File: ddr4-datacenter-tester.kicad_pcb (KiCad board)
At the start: 8 copper layers, 152.9 x 90 mm, 379 parts, among them IC1 TPS54561, IC3 TPD8S009DSMR, J1 0878311420, J10 61300311121, J3 DC_SOCKET, J4 WE_629105150521, J5 2309409-1, J6 685119134923, J7 1140084168, J8 61300311121, Q2 BSS138APW, Q3 BSS138APW, Q4 BSS138APW, Q5 BSS138APW, Q6 BSS138APW, Q7 BSS138APW, Q8 BSS138APW, U1 XC7K70T-FBG484, U10 LM3881MME_NOPB, U11 S27KL0641DABHI023, U12 TPS62823DLCT, U13 XC7K160T-2FFG676C, U14 2199155-1, U15 XC7K160T-FFG676, U16 XC7K70T-FBG484, U2 ASFLMB-100.000MHZ-XY-T, U3 S25FL128SAGNFI000, U4 TPS65296, U5 TPS62823DLCT, U6 KSZ9031RNXCA, U7 FT4232HQ, U8 SRST, U9 TPS62823DLCT, Y1 ABM8G-25.000MHZ-18-D2Y-T, Y2 ABM8G-12.000MHZ-18-D2Y-T

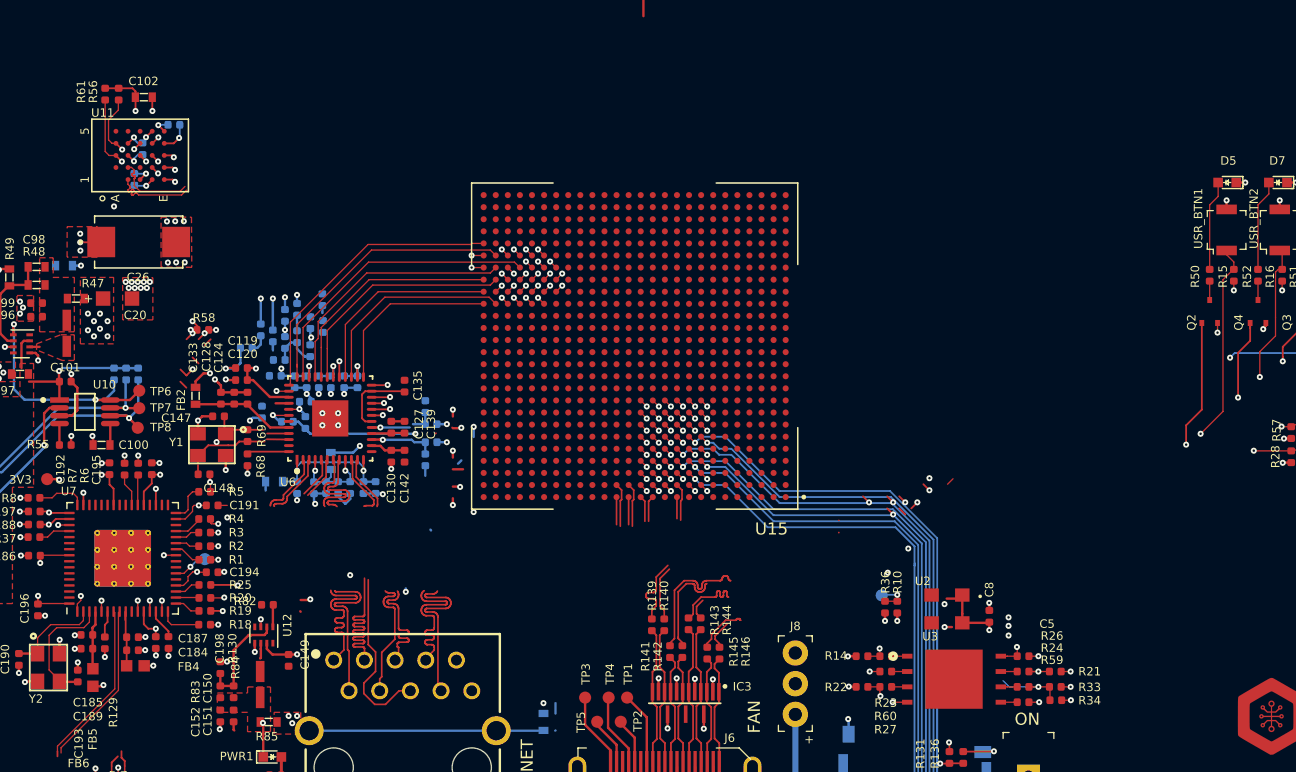
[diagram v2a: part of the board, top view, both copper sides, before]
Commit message: Connect QSPI (fix), GPIOs, JTAG, HR, UART
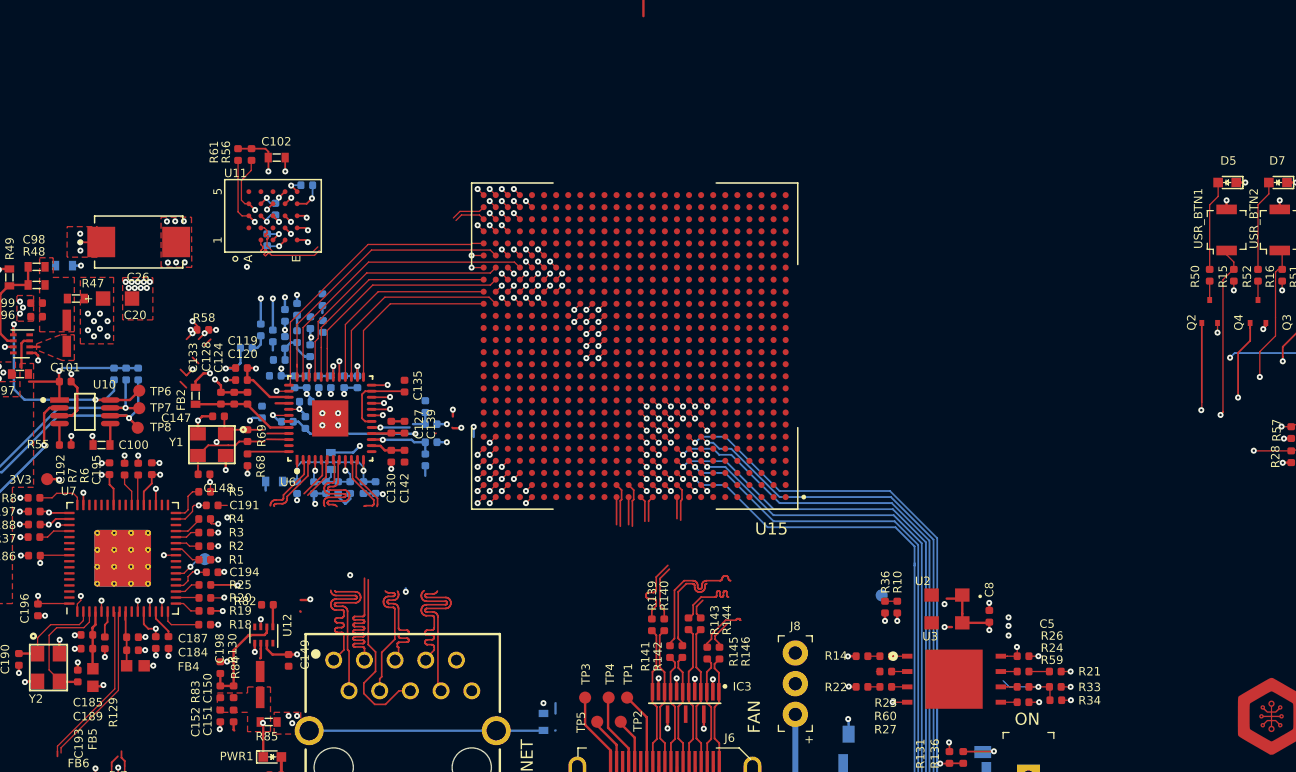
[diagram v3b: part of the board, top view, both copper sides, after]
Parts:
- moved C102 12.1 mm to (154.0, 74.5)
- moved C103 12.1 mm to (156.5, 76.7)
- moved C104 12.1 mm to (153.2, 81.3)
- moved C105 12.1 mm to (153.9, 78.7)
- moved R56 12.1 mm to (151.9, 74.2)
- moved R61 12.1 mm to (150.8, 74.2)
- moved U11 12.1 mm to (153.7, 79.3)
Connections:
- U15 pad A22: Net-(U15-PadA22) -> QSPI_DQ3
- U15 pad A25: Net-(U15-PadA25) -> QSPI_DQ1
- U15 pad AC24: Net-(U15-PadAC24) -> HR_RST
- U15 pad AC26: Net-(U15-PadAC26) -> HR_CS
- U15 pad AD23: Net-(U15-PadAD23) -> HR_RW
- U15 pad AD24: Net-(U15-PadAD24) -> HR_DQ7
- U15 pad AD25: Net-(U15-PadAD25) -> HR_DQ1
- U15 pad AD26: Net-(U15-PadAD26) -> HR_CKP
- U15 pad AE22: Net-(U15-PadAE22) -> HR_DQ3
- U15 pad AE23: Net-(U15-PadAE23) -> HR_DQ0
- U15 pad AE25: Net-(U15-PadAE25) -> HR_DQ6
- U15 pad AE26: Net-(U15-PadAE26) -> HR_CKN
- U15 pad AF23: Net-(U15-PadAF23) -> HR_DQ4
- U15 pad AF24: Net-(U15-PadAF24) -> HR_DQ2
- U15 pad AF25: Net-(U15-PadAF25) -> HR_DQ5
- U15 pad B22: Net-(U15-PadB22) -> QSPI_DQ2
- U15 pad B24: Net-(U15-PadB24) -> QSPI_DQ0
- U15 pad B25: Net-(U15-PadB25) -> PUDC_B
- U15 pad B26: Net-(U15-PadB26) -> EMCCLK
- U15 pad C23: Net-(U15-PadC23) -> FCS_B
- U15 pad C24: Net-(U15-PadC24) -> AUX_JTAG_TCK
- U15 pad C26: Net-(U15-PadC26) -> AUX_JTAG_TDO
- U15 pad D11: FCS_B -> Net-(U15-PadD11)
- U15 pad D24: Net-(U15-PadD24) -> AUX_JTAG_TDI
- U15 pad D25: Net-(U15-PadD25) -> AUX_JTAG_TMS
- U15 pad D26: Net-(U15-PadD26) -> UART1_TX
- U15 pad E11: PUDC_B -> Net-(U15-PadE11)
- U15 pad E25: Net-(U15-PadE25) -> UART1_RX
- U15 pad E26: Net-(U15-PadE26) -> UART0_TX
- U15 pad F10: QSPI_DQ1 -> Net-(U15-PadF10)
- U15 pad F25: Net-(U15-PadF25) -> UART0_RX
- U15 pad G10: QSPI_DQ0 -> Net-(U15-PadG10)
- U15 pad G9: QSPI_DQ2 -> Net-(U15-PadG9)
- U15 pad H8: QSPI_DQ3 -> Net-(U15-PadH8)
- U15 pad N16: Net-(U15-PadN16) -> USR_BTN1
- U15 pad N17: Net-(U15-PadN17) -> USR_LED1
- U15 pad P16: Net-(U15-PadP16) -> USR_LED5
- U15 pad R16: Net-(U15-PadR16) -> USR_LED2
- U15 pad R17: Net-(U15-PadR17) -> USR_BTN4
- U15 pad T17: Net-(U15-PadT17) -> USR_LED4
- U15 pad T18: Net-(U15-PadT18) -> USR_BTN3
- U15 pad U16: Net-(U15-PadU16) -> USR_LED3
- U15 pad U17: Net-(U15-PadU17) -> USR_BTN2
- U16 pad AA14: HR_DQ2 -> Net-(U16-PadAA14)
- U16 pad AA15: HR_DQ1 -> Net-(U16-PadAA15)
- U16 pad AA16: HR_CS -> Net-(U16-PadAA16)
- U16 pad AA18: UART0_RX -> Net-(U16-PadAA18)
- U16 pad AA20: UART1_TX -> Net-(U16-PadAA20)
- U16 pad AB15: HR_CKP -> Net-(U16-PadAB15)
- U16 pad AB16: HR_CKN -> Net-(U16-PadAB16)
- U16 pad AB17: AUX_JTAG_RST -> Net-(U16-PadAB17)
- U16 pad AB18: UART0_TX -> Net-(U16-PadAB18)
- U16 pad AB20: UART1_RX -> Net-(U16-PadAB20)
- U16 pad F19: QSPI_DQ3 -> Net-(U16-PadF19)
- U16 pad G18: QSPI_DQ2 -> Net-(U16-PadG18)
- U16 pad H18: QSPI_DQ0 -> Net-(U16-PadH18)
- U16 pad H19: QSPI_DQ1 -> Net-(U16-PadH19)
- U16 pad J21: TMDS_D2_P -> Net-(U16-PadJ21)
- U16 pad J22: TMDS_D2_N -> Net-(U16-PadJ22)
- U16 pad K21: TMDS_D1_P -> Net-(U16-PadK21)
- U16 pad K22: TMDS_D1_N -> Net-(U16-PadK22)
- U16 pad L16: FCS_B -> Net-(U16-PadL16)
- U16 pad L19: GCLK100 -> Net-(U16-PadL19)
- U16 pad P21: TMDS_D0_P -> Net-(U16-PadP21)
- U16 pad P22: TMDS_D0_N -> Net-(U16-PadP22)
- U16 pad R21: TMDS_CLK_P -> Net-(U16-PadR21)
- U16 pad R22: TMDS_CLK_N -> Net-(U16-PadR22)
- U16 pad V15: HR_DQ5 -> Net-(U16-PadV15)
- U16 pad V17: HR_RST -> Net-(U16-PadV17)
- U16 pad W14: HR_DQ3 -> Net-(U16-PadW14)
- U16 pad W15: HR_DQ0 -> Net-(U16-PadW15)
- U16 pad W17: HR_DQ7 -> Net-(U16-PadW17)
- U16 pad W20: AUX_JTAG_TDI -> Net-(U16-PadW20)
- U16 pad W21: AUX_JTAG_TDO -> Net-(U16-PadW21)
- U16 pad W22: AUX_JTAG_TCK -> Net-(U16-PadW22)
- U16 pad Y14: HR_DQ4 -> Net-(U16-PadY14)
- U16 pad Y16: HR_DQ6 -> Net-(U16-PadY16)
- U16 pad Y17: HR_RW -> Net-(U16-PadY17)
- U16 pad Y21: AUX_JTAG_TMS -> Net-(U16-PadY21)
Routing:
- net QSPI_DQ3: track 30.4 -> 2.40 mm, vias 3 -> 1
- net QSPI_DQ2: track 25.6 -> 1.76 mm, vias 3 -> 1
- net QSPI_DQ1: track 23.4 -> 1.00 mm, vias 4 -> 1
- net FCS_B: track 22.8 -> 1.71 mm, vias 2 -> 1
- net PUDC_B: track 18.0 -> 1.72 mm, vias 3 -> 1
- net HR_RW: track 4.13 -> 13.3 mm, vias 1 -> 2
- net HR_DQ3: track 4.60 -> 13.7 mm, vias 1 -> 2
- net HR_RST: track 11.0 -> 19.6 mm, vias 1 -> 2
- net HR_DQ0: track 3.44 -> 11.5 mm, vias 1 -> 2
- net HR_DQ7: track 3.17 -> 10.8 mm, vias 1 -> 2
- net HR_DQ4: track 4.93 -> 12.1 mm, vias 1 -> 2
- net QSPI_DQ0: track 34.0 -> 27.1 mm, vias 3 -> 2
- net USR_BTN4: track 18.9 -> 25.6 mm, vias 1 -> 2
- net HR_DQ1: track 8.80 -> 15.5 mm, vias 1 -> 2
- net HR_CS: track 11.9 -> 18.2 mm, vias 1 -> 2
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
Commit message: Add BGA fanout-WIP
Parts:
- removed J5: 2309409-1, ddr4-datacenter-tester-footprints:TE_2309409-1
- removed U1, U16: XC7K70T-FBG484, ddr4-datacenter-tester-footprints:BGA484C100P22X22_2300X2300X244N
- removed U13: XC7K160T-2FFG676C, antmicro-footprints:BGA676C100P26X26_2700X2700X254
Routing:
- net Net-(U15-PadY11): track 0.00 -> 44.2 mm, vias 0 -> 1
- net Net-(U15-PadY10): track 0.00 -> 42.8 mm, vias 0 -> 1
- net Net-(U15-PadY8): track 0.00 -> 40.1 mm, vias 0 -> 1
- net Net-(U15-PadV11): track 0.00 -> 39.3 mm, vias 0 -> 1
- net Net-(U15-PadW11): track 0.00 -> 38.8 mm, vias 0 -> 1
- net Net-(U15-PadY7): track 0.00 -> 38.0 mm, vias 0 -> 1
- net VDDQ: track 20.4 -> 58.2 mm, vias 16 -> 33
- net Net-(U15-PadW10): track 0.00 -> 35.9 mm, vias 0 -> 1
- net Net-(U15-PadV9): track 0.00 -> 34.8 mm, vias 0 -> 1
- net Net-(U15-PadW9): track 0.00 -> 34.2 mm, vias 0 -> 1
- net Net-(U15-PadU6): track 0.00 -> 33.3 mm, vias 0 -> 1
- net Net-(U15-PadW6): track 0.00 -> 31.5 mm, vias 0 -> 1
- net Net-(U15-PadV6): track 0.00 -> 31.5 mm, vias 0 -> 1
- net Net-(U15-PadU5): track 0.00 -> 31.4 mm, vias 0 -> 1
- net Net-(U15-PadV8): track 0.00 -> 31.1 mm, vias 0 -> 1
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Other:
- board text added: "DQ_S lines- BANK32"
- board text added: "DQ_S lines- BANK33"
- board text added: "DQ_S lines- BANK34"

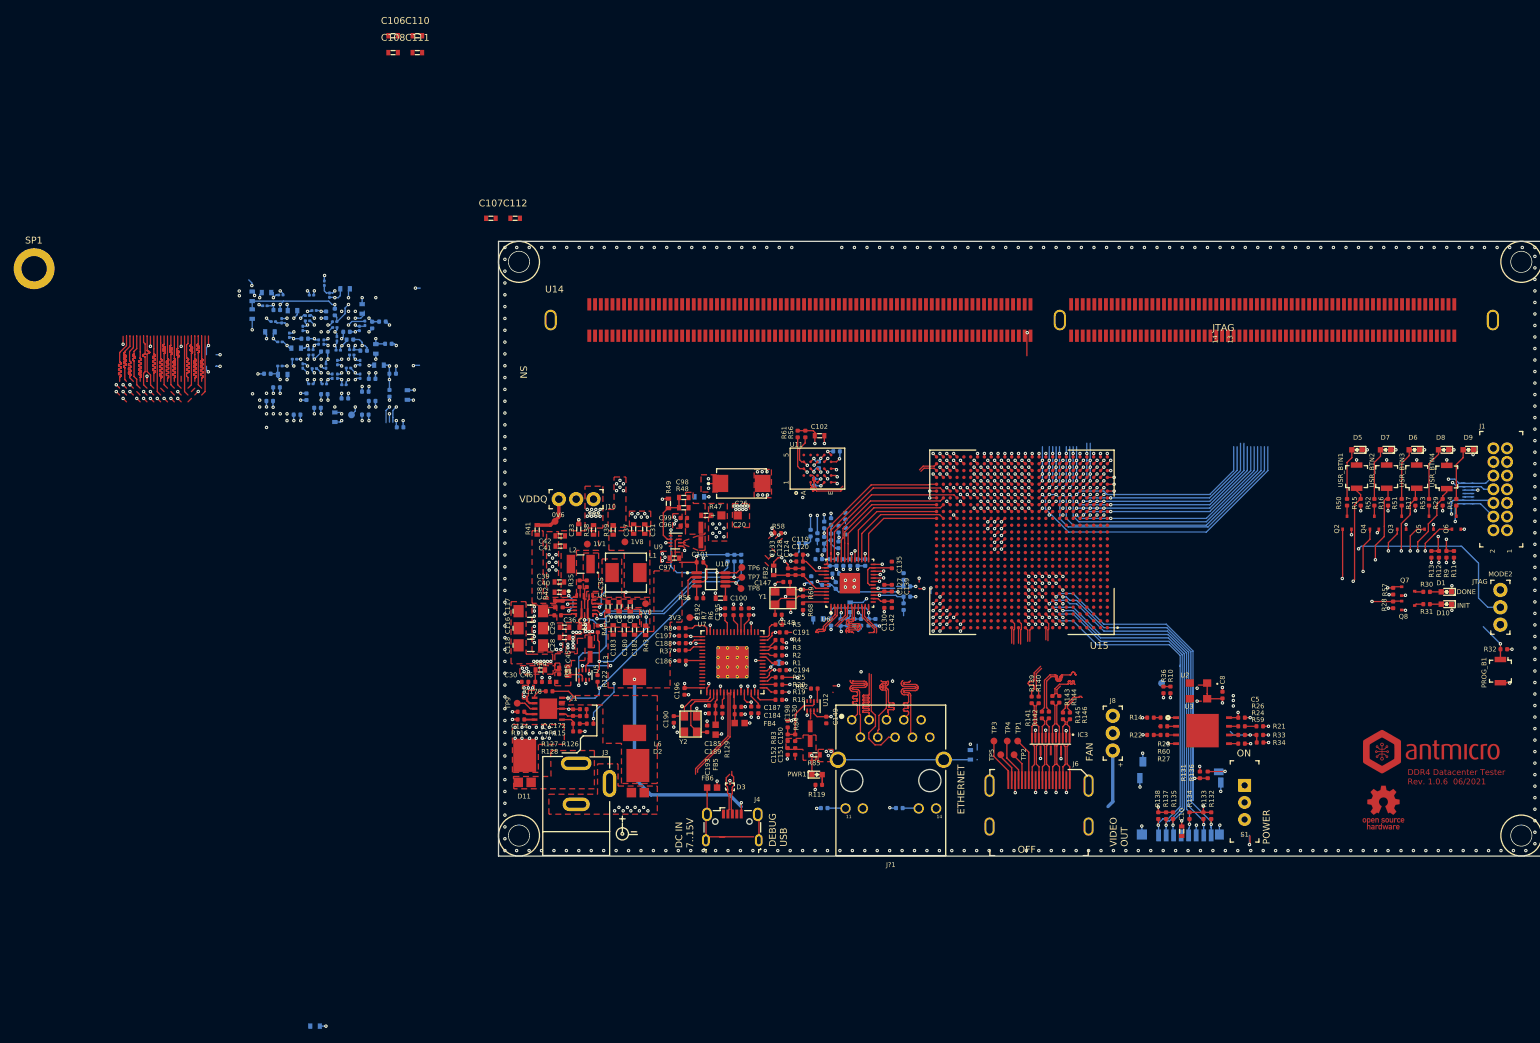
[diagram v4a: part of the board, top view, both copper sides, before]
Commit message: Add DDR4 fanout
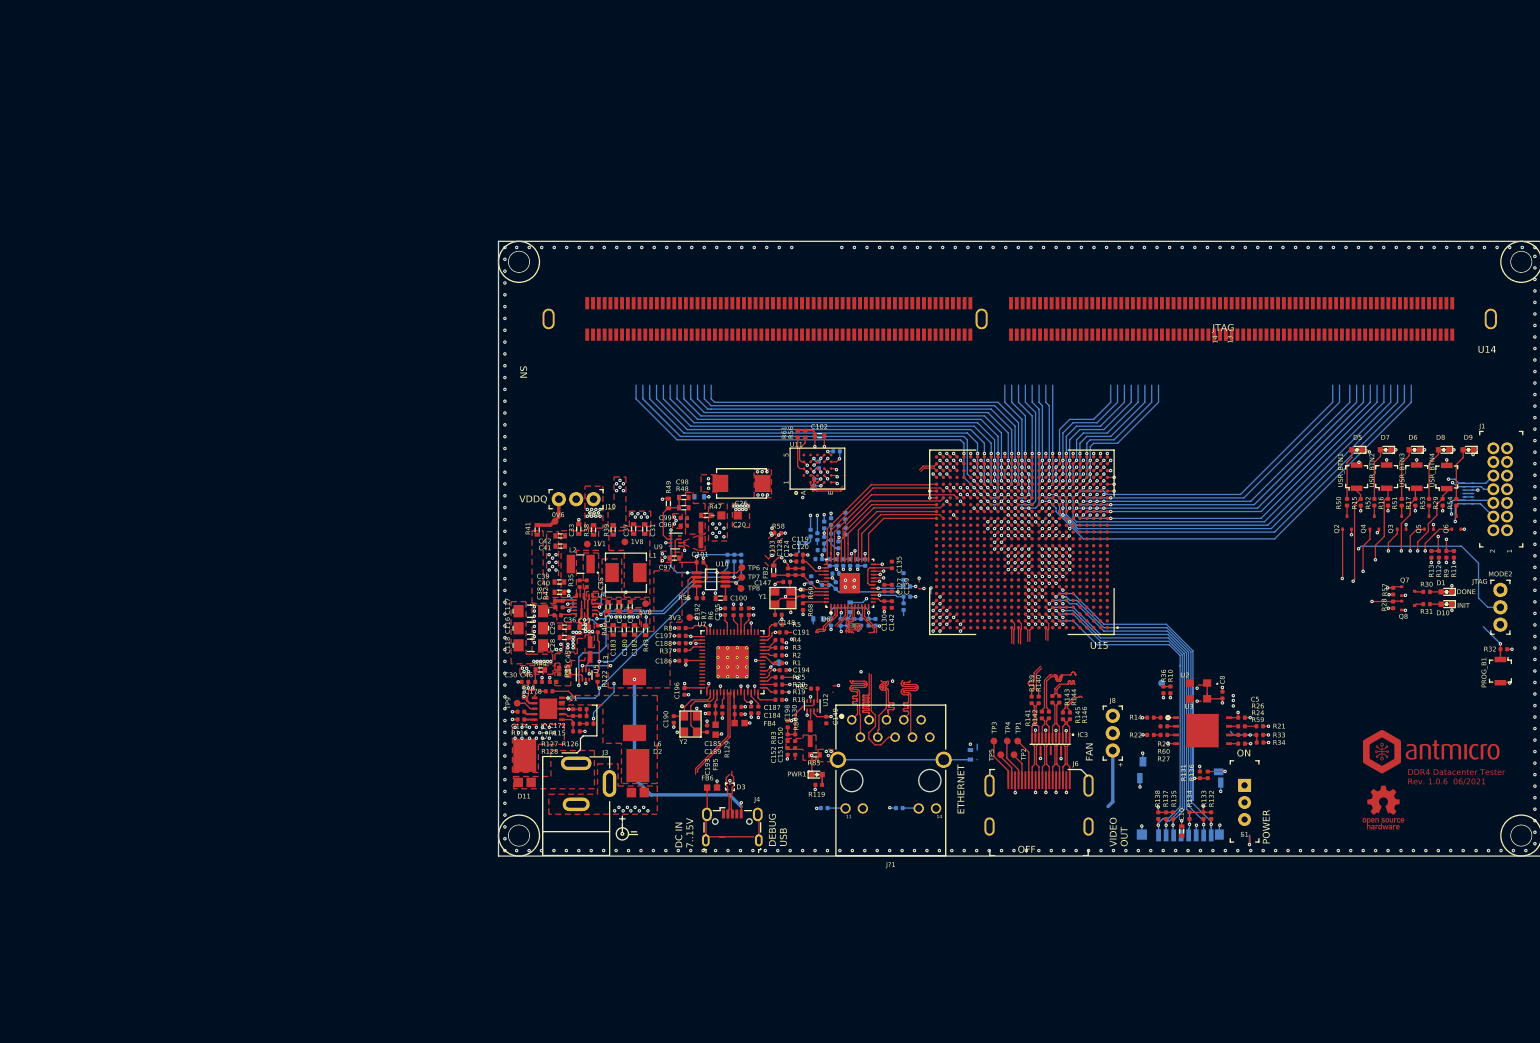
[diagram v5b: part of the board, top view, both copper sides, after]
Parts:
- removed C106, C107, C108, C110, C111, C112, C113: C_10n_0603, ddr4-datacenter-tester-footprints:0603-cap
- removed C11, C143, C21, C32, C34, C43, C44, C47, C48, C49, C50, C51, C52, C53, C54, C55, C56, C57, C58, C59, C60, C61, C62, C63, C64, C65, C66, C67, C68, C69, C70, C71, C72, C73, C74, C75, C76, C77, C9: C_100n_0201, ddr4-datacenter-tester-footprints:0201-res
- removed C114, C115: C_100n_0402_6V3, ddr4-datacenter-tester-footprints:0402-cap
- removed C12, C15, C18, C22, C23, C24, C25, C3, C6: C_47u_0603, ddr4-datacenter-tester-footprints:0603-cap
- removed C13: C_470n_0402, ddr4-datacenter-tester-footprints:0402-cap
- removed C14, C16, C17, C19, C7, C78, C79, C80, C81, C82, C83, C84, C85, C86, C87, C88, C89, C90, C91, C92, C93, C94, C95: C_4u7_0402, ddr4-datacenter-tester-footprints:0402-cap
- removed EMCCLK1: test, ddr4-datacenter-tester-footprints:Testpoint_smd_1mm
- removed R63, R64: R_120R_0603, ddr4-datacenter-tester-footprints:0603-res
- removed R65, R66: R_1k_0603, ddr4-datacenter-tester-footprints:0603-res
- removed SP1: 9774050151, ddr4-datacenter-tester-footprints:9774050151
- moved U14 126.4 mm to (246.6, 55.1), turned to 180 degrees
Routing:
- net Net-(U15-PadV14): track 0.71 -> 84.1 mm
- net Net-(U15-PadY15): track 0.71 -> 67.2 mm
- net Net-(U15-PadW15): track 0.71 -> 66.4 mm
- net GND: track 247.8 -> 182.8 mm, vias 489 -> 455
- net Net-(U15-PadY16): track 0.71 -> 64.3 mm
- net Net-(U15-PadV16): track 0.71 -> 63.3 mm
- net Net-(U15-PadW16): track 0.71 -> 62.6 mm
- net Net-(U15-PadY17): track 0.71 -> 60.7 mm
- net Net-(U15-PadAA18): track 0.71 -> 60.1 mm
- net Net-(U15-PadAA17): track 0.71 -> 60.1 mm
- net Net-(U15-PadAA15): track 0.71 -> 59.3 mm
- net Net-(U15-PadV17): track 0.71 -> 59.2 mm
- net Net-(U15-PadAB19): track 0.71 -> 59.1 mm
- net Net-(U15-PadAA14): track 0.71 -> 58.9 mm
- net Net-(U15-PadAB17): track 0.71 -> 58.7 mm
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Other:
- copper layers 8 -> 10
